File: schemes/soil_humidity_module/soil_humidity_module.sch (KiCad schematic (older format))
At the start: 10 parts, among them Q1 IRL540N, Q2 BC547, U1 nRF24L01P, U2 SEN0193

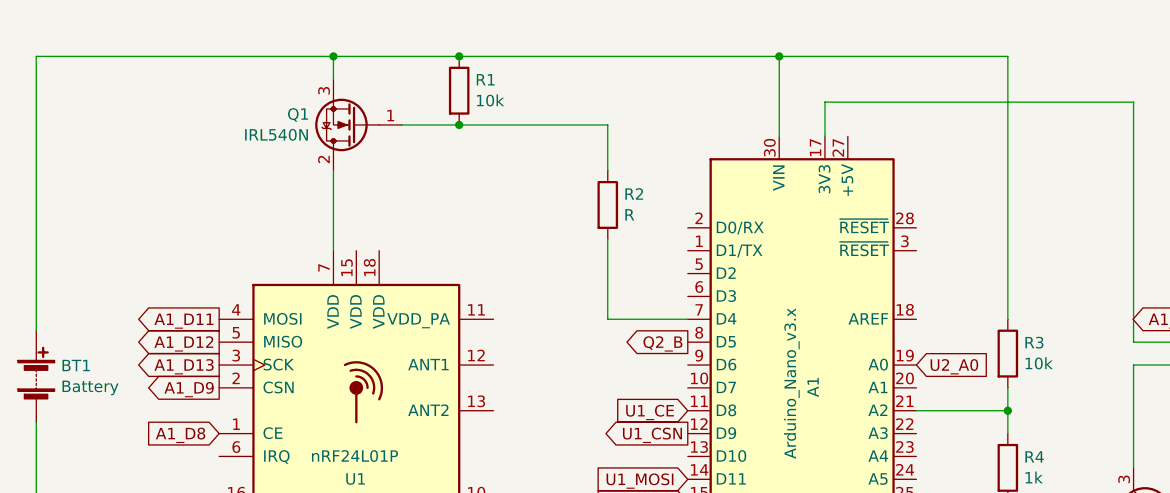
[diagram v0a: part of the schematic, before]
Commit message: Added weekdays selection popup. Changed front-end file structure
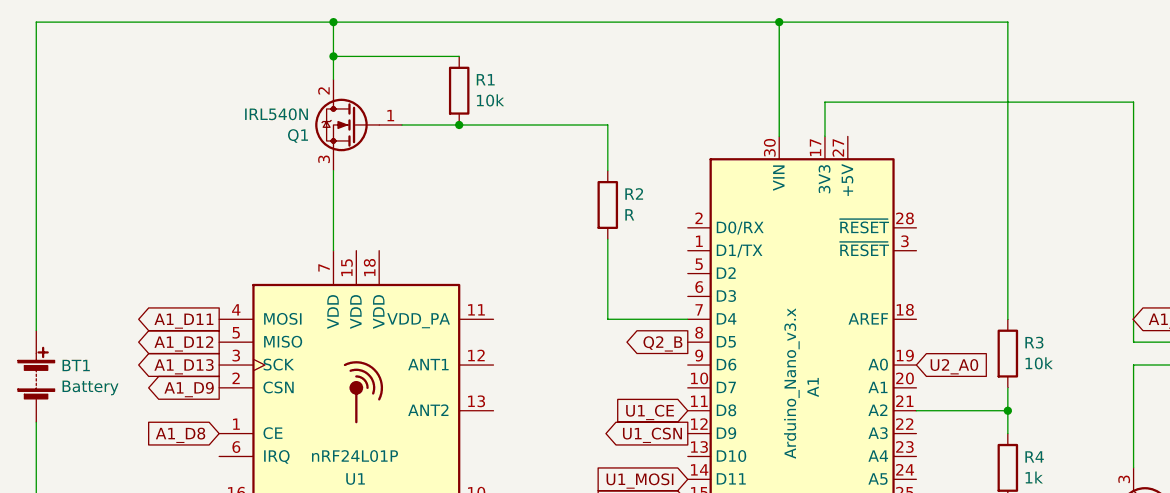
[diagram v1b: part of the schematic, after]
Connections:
- net at A1.30 (VIN), BT1.1 (+), R1.1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: now also Q1.2 (D); no longer Q1.3 (S)
- net at U1.7 (VDD): now also Q1.3 (S); no longer Q1.2 (D)
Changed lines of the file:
@@
 U1_CE
-Wire Wire Line
-	3300 2600 3300 3800
 Wire Wire Line
 	3300 5150 4600 5150
@@
 	6650 5150 6650 4950
 Connection ~ 4600 5150
-Wire Wire Line
-	6550 2600 6550 2950
 $Comp
 L Device:R R3
@@
 	7550 5150 7550 4550
 Connection ~ 6650 5150
-Connection ~ 6550 2600
-Wire Wire Line
-	7550 2600 7550 3750
 Wire Wire Line
 	7550 4050 7550 4150
@@
 Wire Wire Line
 	5800 3750 6150 3750
-Wire Wire Line
-	3300 2600 4600 2600
-Connection ~ 4600 2600
-Wire Wire Line
-	4600 2600 5150 2600
 $Comp
 L Device:R R1
@@
 	1    0    0    -1
 $EndComp
-Connection ~ 5150 2600
 Wire Wire Line
 	4600 2700 4600 2600
@@
 F 3 "https://www.infineon.com/dgdl/irl540npbf.pdf?fileId=5546d462533600a40153565fc2a62567" H 4700 2900 50  0001 L CNN
 	1    4700 2900
-	-1   0    0    1
+	-1   0    0    -1
 $EndComp
 Wire Wire Line
@@
 Wire Wire Line
 	4600 5150 6650 5150
-Wire Wire Line
-	5150 2600 6550 2600
 $Comp
 L trial:SEN0193 U2
@@
 Text GLabel 7150 3950 2    50   Input ~ 0
 U2_A0
-Wire Wire Line
-	6550 2600 7550 2600
 Wire Wire Line
 	6650 5150 7550 5150
@@
 	1    0    0    -1
 $EndComp
+Wire Wire Line
+	3300 2450 4600 2450
+Wire Wire Line
+	3300 2450 3300 3800
+Wire Wire Line
+	7550 2450 7550 3750
+Wire Wire Line
+	6550 2450 6550 2950
+Connection ~ 6550 2450
+Wire Wire Line
+	6550 2450 7550 2450
+Wire Wire Line
+	5150 2600 4600 2600
+Wire Wire Line
+	4600 2600 4600 2450
+Connection ~ 4600 2600
+Connection ~ 4600 2450
+Wire Wire Line
+	4600 2450 6550 2450
 $EndSCHEMATC

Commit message: Updated schemes and technical sheets
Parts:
- removed R2: R, symbol Device:R
- R1: value 10k -> 100k
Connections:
- net at A1.18 (AREF): now also A1.27 (+5V)
- net at A1.29 (GND): now also A1.4 (GND), BT1.2 (-), Q1.3 (S), Q2.3 (E), R1.2, R4.2
- net at A1.30 (VIN), BT1.1 (+), R3.1: now also U1.7 (VDD); no longer Q1.2 (D), R1.1
- net at A1.7 (D4): now also Q1.1 (G), R1.1
- net at U2.1 (GND): now also Q2.1 (C); no longer Q2.3 (E)
- net U1_D5 renamed A1_D5
- new net: Q1.2 (D), U1.8 (VSS)
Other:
- moved on the sheet: Q1, R1, U1
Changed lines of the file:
@@
 Text GLabel 6150 4550 0    50   Input ~ 0
 U1_MISO
-Text GLabel 4100 3850 0    50   Output ~ 0
-A1_D12
-Text GLabel 4100 3950 0    50   Output ~ 0
-A1_D13
-Text GLabel 6150 4650 0    50   Input ~ 0
+Text GLabel 6150 4650 0    50   Output ~ 0
 U1_SCK
-Text GLabel 6150 4450 0    50   Input ~ 0
+Text GLabel 6150 4450 0    50   Output ~ 0
 U1_MOSI
-Text GLabel 4100 3750 0    50   Output ~ 0
-A1_D11
-Text GLabel 4100 4050 0    50   Output ~ 0
-A1_D9
 Text GLabel 6150 4250 0    50   Output ~ 0
 U1_CSN
-Text GLabel 4100 4250 0    50   Input ~ 0
-A1_D8
-Text GLabel 6150 4150 0    50   Input ~ 0
+Text GLabel 6150 4150 0    50   Output ~ 0
 U1_CE
-Wire Wire Line
-	3300 5150 4600 5150
-Wire Wire Line
-	3300 4200 3300 5150
-Wire Wire Line
-	4600 5050 4600 5150
-Wire Wire Line
-	6650 5150 6650 4950
-Connection ~ 4600 5150
 $Comp
 L Device:R R3
@@
 $EndComp
 Wire Wire Line
-	7550 5150 7550 4550
-Connection ~ 6650 5150
-Wire Wire Line
 	7550 4050 7550 4150
 Connection ~ 7550 4150
@@
 	7550 4150 7550 4250
 Wire Wire Line
-	5800 3750 6150 3750
-$Comp
-L Device:R R1
-U 1 1 5F31B617
-P 5150 2750
-F 0 "R1" H 5220 2796 50  0000 L CNN
-F 1 "10k" H 5220 2705 50  0000 L CNN
-F 2 "" V 5080 2750 50  0001 C CNN
-F 3 "~" H 5150 2750 50  0001 C CNN
-	1    5150 2750
-	1    0    0    -1
-$EndComp
-Wire Wire Line
-	4600 2700 4600 2600
-Wire Wire Line
-	4600 3100 4600 3450
-$Comp
-L trial:IRL540N Q1
-U 1 1 5F29F1A2
-P 4700 2900
-F 0 "Q1" H 4905 2854 50  0000 L CNN
-F 1 "IRL540N" H 4905 2945 50  0000 L CNN
-F 2 "Package_TO_SOT_THT:TO-220-3_Vertical" H 4950 2825 50  0001 L CIN
-F 3 "https://www.infineon.com/dgdl/irl540npbf.pdf?fileId=5546d462533600a40153565fc2a62567" H 4700 2900 50  0001 L CNN
-	1    4700 2900
-	-1   0    0    -1
-$EndComp
-Wire Wire Line
-	4900 2900 5150 2900
-Wire Wire Line
-	5800 2900 5800 3100
-Connection ~ 5150 2900
-Wire Wire Line
-	5150 2900 5800 2900
-$Comp
-L Device:R R2
-U 1 1 5F322358
-P 5800 3250
-F 0 "R2" H 5870 3296 50  0000 L CNN
-F 1 "R" H 5870 3205 50  0000 L CNN
-F 2 "" V 5730 3250 50  0001 C CNN
-F 3 "~" H 5800 3250 50  0001 C CNN
-	1    5800 3250
-	1    0    0    -1
-$EndComp
-Wire Wire Line
-	5800 3400 5800 3750
-Wire Wire Line
 	7150 4150 7550 4150
-Wire Wire Line
-	4600 5150 6650 5150
 $Comp
 L trial:SEN0193 U2
@@
 U2_A0
 Wire Wire Line
-	6650 5150 7550 5150
-Wire Wire Line
 	6750 2950 6750 2800
 Wire Wire Line
@@
 F 3 "http://www.fairchildsemi.com/ds/BC/BC547.pdf" H 8200 4600 50  0001 L CNN
 	1    8200 4600
-	-1   0    0    1
+	-1   0    0    -1
 $EndComp
-Text GLabel 8400 4600 2    50   Input ~ 0
-U1_D5
 Text GLabel 6150 3850 0    50   Output ~ 0
 Q2_B
 Wire Wire Line
-	8100 4800 8100 5150
-Wire Wire Line
 	6750 2800 8100 2800
 Wire Wire Line
-	7550 5150 8100 5150
-Connection ~ 7550 5150
+	3300 2650 4650 2650
+Wire Wire Line
+	4650 5300 5100 5300
+Connection ~ 4650 5300
+Wire Wire Line
+	3300 5300 4650 5300
+Wire Wire Line
+	4650 5300 4650 5200
+Wire Wire Line
+	5100 5300 6650 5300
+Connection ~ 5100 5300
+Wire Wire Line
+	5100 5000 5550 5000
+Connection ~ 5100 5000
+Wire Wire Line
+	4950 5000 5100 5000
+$Comp
+L trial:IRL540N Q1
+U 1 1 5F29F1A2
+P 4750 5000
+F 0 "Q1" H 4955 4954 50  0000 L CNN
+F 1 "IRL540N" H 4955 5045 50  0000 L CNN
+F 2 "Package_TO_SOT_THT:TO-220-3_Vertical" H 5000 4925 50  0001 L CIN
+F 3 "https://www.infineon.com/dgdl/irl540npbf.pdf?fileId=5546d462533600a40153565fc2a62567" H 4750 5000 50  0001 L CNN
+	1    4750 5000
+	-1   0    0    -1
+$EndComp
 $Comp
 L RF:nRF24L01P U1
 U 1 1 5F26A887
-P 4700 4250
-F 0 "U1" H 4650 4050 50  0000 L CNN
-F 1 "nRF24L01P" H 4500 4150 50  0000 L CNN
-F 2 "Package_DFN_QFN:QFN-20-1EP_4x4mm_P0.5mm_EP2.5x2.5mm" V 4609 5093 50  0001 L CIN
-F 3 "http://www.nordicsemi.com/eng/content/download/2726/34069/file/nRF24L01P_Product_Specification_1_0.pdf" H 4700 4350 50  0001 C CNN
-	1    4700 4250
+P 4750 3900
+F 0 "U1" H 4700 3700 50  0000 L CNN
+F 1 "nRF24L01P" H 4550 3800 50  0000 L CNN
+F 2 "Package_DFN_QFN:QFN-20-1EP_4x4mm_P0.5mm_EP2.5x2.5mm" V 4659 4743 50  0001 L CIN
+F 3 "http://www.nordicsemi.com/eng/content/download/2726/34069/file/nRF24L01P_Product_Specification_1_0.pdf" H 4750 4000 50  0001 C CNN
+	1    4750 3900
+	1    0    0    -1
+$EndComp
+$Comp
+L Device:R R1
+U 1 1 5F31B617
+P 5100 5150
+F 0 "R1" H 5170 5196 50  0000 L CNN
+F 1 "100k" H 5170 5105 50  0000 L CNN
+F 2 "" V 5030 5150 50  0001 C CNN
+F 3 "~" H 5100 5150 50  0001 C CNN
+	1    5100 5150
 	1    0    0    -1
 $EndComp
 Wire Wire Line
-	3300 2450 4600 2450
+	4650 4700 4650 4800
+Text GLabel 4150 3900 0    50   Input ~ 0
+A1_D8
+Text GLabel 4150 3700 0    50   Input ~ 0
+A1_D9
+Text GLabel 4150 3400 0    50   Input ~ 0
+A1_D11
+Text GLabel 4150 3600 0    50   Input ~ 0
+A1_D13
+Text GLabel 4150 3500 0    50   Output ~ 0
+A1_D12
 Wire Wire Line
-	3300 2450 3300 3800
+	5550 3750 6150 3750
 Wire Wire Line
-	7550 2450 7550 3750
+	6650 4950 6650 5300
+Connection ~ 6650 5300
 Wire Wire Line
-	6550 2450 6550 2950
-Connection ~ 6550 2450
+	6650 5300 6750 5300
 Wire Wire Line
-	6550 2450 7550 2450
+	7550 4550 7550 5300
+Connection ~ 7550 5300
 Wire Wire Line
-	5150 2600 4600 2600
+	7550 5300 8100 5300
 Wire Wire Line
-	4600 2600 4600 2450
-Connection ~ 4600 2600
-Connection ~ 4600 2450
+	8100 4800 8100 5300
+Text GLabel 8400 4600 2    50   Input ~ 0
+A1_D5
 Wire Wire Line
-	4600 2450 6550 2450
+	3300 4200 3300 5300
+Wire Wire Line
+	4650 2650 6550 2650
+Connection ~ 4650 2650
+Wire Wire Line
+	4650 2650 4650 3100
+Connection ~ 6550 2650
+Wire Wire Line
+	6550 2650 6550 2950
+Wire Wire Line
+	7550 2650 7550 3750
+Wire Wire Line
+	3300 2650 3300 3800
+Wire Wire Line
+	5550 3750 5550 5000
+Wire Wire Line
+	6750 4950 6750 5300
+Connection ~ 6750 5300
+Wire Wire Line
+	6750 5300 7550 5300
+Wire Wire Line
+	6550 2650 7550 2650
+Wire Wire Line
+	6850 2950 6850 2900
+Wire Wire Line
+	6850 2900 7350 2900
+Wire Wire Line
+	7350 2900 7350 3750
+Wire Wire Line
+	7350 3750 7150 3750
 $EndSCHEMATC

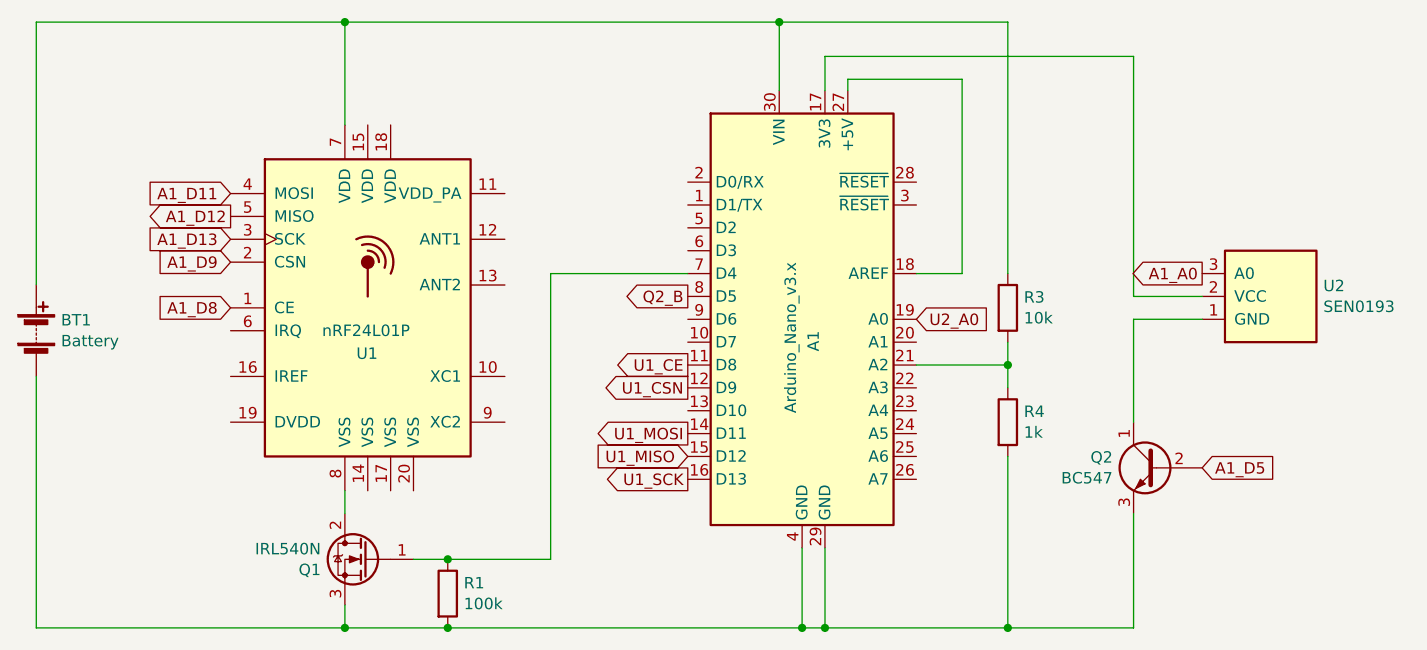
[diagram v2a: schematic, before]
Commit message: Improving soil humidity module scheme and pcb
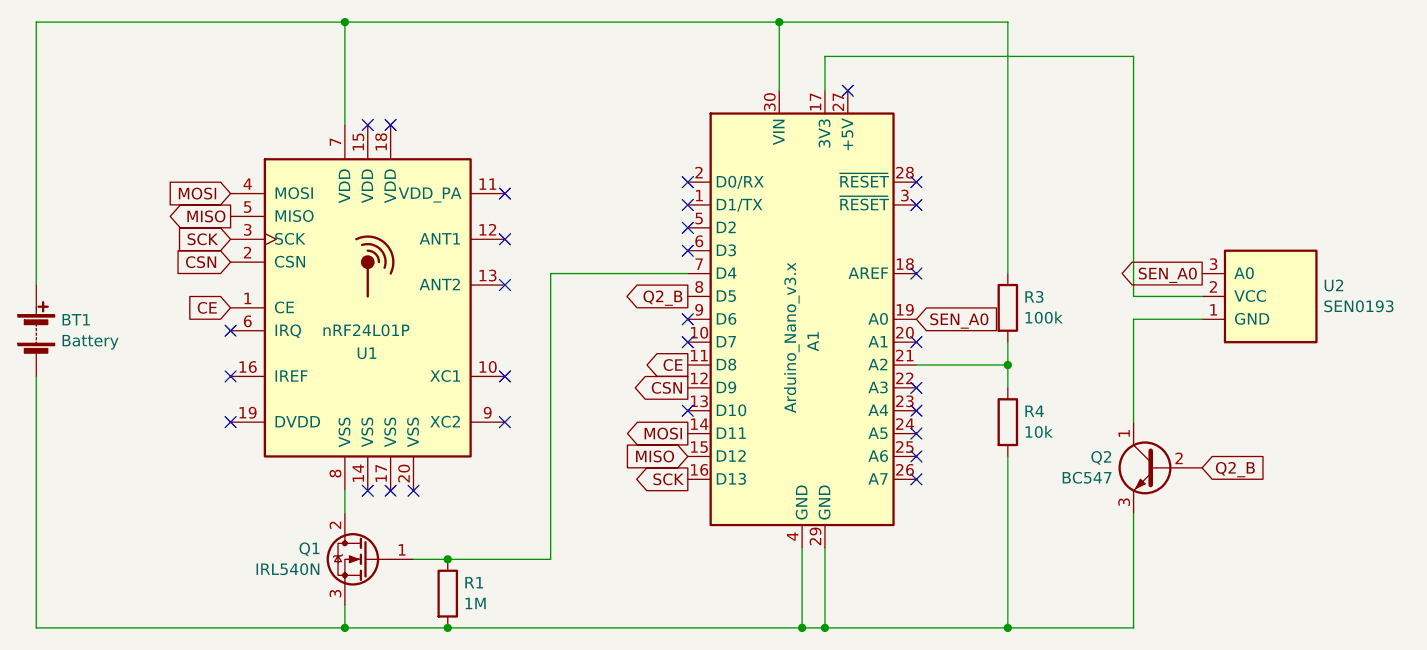
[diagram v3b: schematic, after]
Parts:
- removed Q1: IRL540N, Package_TO_SOT_THT:TO-220-3_Vertical, symbol trial:IRL540N
- added Q1: IRL540N, Package_TO_SOT_THT:TO-220-3_Vertical, symbol soil_humidity_module:IRL540N
- BT1: footprint (none) -> Connector_AMASS:AMASS_XT30U-F_1x02_P5.0mm_Vertical
- R1: value 100k -> 1M; footprint (none) -> Resistor_SMD:R_0805_2012Metric_Pad1.15x1.40mm_HandSolder
- R3: value 10k -> 100k; footprint (none) -> Resistor_SMD:R_0805_2012Metric_Pad1.15x1.40mm_HandSolder
- R4: value 1k -> 10k; footprint (none) -> Resistor_SMD:R_0805_2012Metric_Pad1.15x1.40mm_HandSolder
- U1: footprint Package_DFN_QFN:QFN-20-1EP_4x4mm_P0.5mm_EP2.5x2.5mm -> Connector_PinHeader_2.54mm:PinHeader_2x04_P2.54mm_Vertical
- U2: footprint (none) -> Connector_JST:JST_EH_B3B-EH-A_1x03_P2.50mm_Vertical
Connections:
- net A1_D5 is gone; now on net Q2_B: Q2.2 (B)
- net U1_CE is gone; now on net CE: A1.11 (D8)
- net U1_CSN is gone; now on net CSN: A1.12 (D9)
- net U1_MISO is gone; now on net MISO: A1.15 (D12)
- net U1_MOSI is gone; now on net MOSI: A1.14 (D11)
- net U1_SCK is gone; now on net SCK: A1.16 (D13)
- net U2_A0 is gone; now on net SEN_A0: A1.19 (A0)
- net at A1.18 (AREF): no longer A1.27 (+5V)
- net at A1.29 (GND), A1.4 (GND), BT1.2 (-)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: now also Q1.3 (S)
- net at A1.7 (D4), R1.1: now also Q1.1 (G)
- net at U1.8 (VSS): now also Q1.2 (D)
- net A1_A0 renamed SEN_A0
- net A1_D11 renamed MOSI
- net A1_D12 renamed MISO
- net A1_D13 renamed SCK
- net A1_D8 renamed CE
- net A1_D9 renamed CSN
- no-connect marks 0 -> 30
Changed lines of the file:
@@
 F 0 "BT1" H 3408 4046 50  0000 L CNN
 F 1 "Battery" H 3408 3955 50  0000 L CNN
-F 2 "" V 3300 4060 50  0001 C CNN
+F 2 "Connector_AMASS:AMASS_XT30U-F_1x02_P5.0mm_Vertical" V 3300 4060 50  0001 C CNN
 F 3 "~" V 3300 4060 50  0001 C CNN
 	1    3300 4000
@@
 $EndComp
 Text GLabel 6150 4550 0    50   Input ~ 0
-U1_MISO
+MISO
 Text GLabel 6150 4650 0    50   Output ~ 0
-U1_SCK
+SCK
 Text GLabel 6150 4450 0    50   Output ~ 0
-U1_MOSI
+MOSI
 Text GLabel 6150 4250 0    50   Output ~ 0
-U1_CSN
+CSN
 Text GLabel 6150 4150 0    50   Output ~ 0
-U1_CE
+CE
 $Comp
 L Device:R R3
@@
 P 7550 3900
 F 0 "R3" H 7620 3946 50  0000 L CNN
-F 1 "10k" H 7620 3855 50  0000 L CNN
-F 2 "" V 7480 3900 50  0001 C CNN
+F 1 "100k" H 7620 3855 50  0000 L CNN
+F 2 "Resistor_SMD:R_0805_2012Metric_Pad1.15x1.40mm_HandSolder" V 7480 3900 50  0001 C CNN
 F 3 "~" H 7550 3900 50  0001 C CNN
 	1    7550 3900
@@
 P 7550 4400
 F 0 "R4" H 7620 4446 50  0000 L CNN
-F 1 "1k" H 7620 4355 50  0000 L CNN
-F 2 "" V 7480 4400 50  0001 C CNN
+F 1 "10k" H 7620 4355 50  0000 L CNN
+F 2 "Resistor_SMD:R_0805_2012Metric_Pad1.15x1.40mm_HandSolder" V 7480 4400 50  0001 C CNN
 F 3 "~" H 7550 4400 50  0001 C CNN
 	1    7550 4400
@@
 F 0 "U2" V 8646 3520 50  0000 R CNN
 F 1 "SEN0193" V 8555 3520 50  0000 R CNN
-F 2 "" H 8500 3450 50  0001 C CNN
+F 2 "Connector_JST:JST_EH_B3B-EH-A_1x03_P2.50mm_Vertical" H 8500 3450 50  0001 C CNN
 F 3 "" H 8500 3450 50  0001 C CNN
 	1    8600 3850
@@
 	8100 3850 8100 2800
 Text GLabel 8400 3750 0    50   Output ~ 0
-A1_A0
+SEN_A0
 Wire Wire Line
 	8100 3850 8400 3850
@@
 	8100 3950 8400 3950
 Text GLabel 7150 3950 2    50   Input ~ 0
-U2_A0
+SEN_A0
 Wire Wire Line
 	6750 2950 6750 2800
@@
 	6750 2800 8100 2800
 Wire Wire Line
-	3300 2650 4650 2650
-Wire Wire Line
 	4650 5300 5100 5300
-Connection ~ 4650 5300
-Wire Wire Line
-	3300 5300 4650 5300
 Wire Wire Line
 	4650 5300 4650 5200
-Wire Wire Line
-	5100 5300 6650 5300
 Connection ~ 5100 5300
 Wire Wire Line
@@
 Wire Wire Line
 	4950 5000 5100 5000
-$Comp
-L trial:IRL540N Q1
-U 1 1 5F29F1A2
-P 4750 5000
-F 0 "Q1" H 4955 4954 50  0000 L CNN
-F 1 "IRL540N" H 4955 5045 50  0000 L CNN
-F 2 "Package_TO_SOT_THT:TO-220-3_Vertical" H 5000 4925 50  0001 L CIN
-F 3 "https://www.infineon.com/dgdl/irl540npbf.pdf?fileId=5546d462533600a40153565fc2a62567" H 4750 5000 50  0001 L CNN
-	1    4750 5000
-	-1   0    0    -1
-$EndComp
 $Comp
 L RF:nRF24L01P U1
@@
 F 0 "U1" H 4700 3700 50  0000 L CNN
 F 1 "nRF24L01P" H 4550 3800 50  0000 L CNN
-F 2 "Package_DFN_QFN:QFN-20-1EP_4x4mm_P0.5mm_EP2.5x2.5mm" V 4659 4743 50  0001 L CIN
+F 2 "Connector_PinHeader_2.54mm:PinHeader_2x04_P2.54mm_Vertical" V 4659 4743 50  0001 L CIN
 F 3 "http://www.nordicsemi.com/eng/content/download/2726/34069/file/nRF24L01P_Product_Specification_1_0.pdf" H 4750 4000 50  0001 C CNN
 	1    4750 3900
@@
 P 5100 5150
 F 0 "R1" H 5170 5196 50  0000 L CNN
-F 1 "100k" H 5170 5105 50  0000 L CNN
-F 2 "" V 5030 5150 50  0001 C CNN
+F 1 "1M" H 5170 5105 50  0000 L CNN
+F 2 "Resistor_SMD:R_0805_2012Metric_Pad1.15x1.40mm_HandSolder" V 5030 5150 50  0001 C CNN
 F 3 "~" H 5100 5150 50  0001 C CNN
 	1    5100 5150
@@
 	4650 4700 4650 4800
 Text GLabel 4150 3900 0    50   Input ~ 0
-A1_D8
+CE
 Text GLabel 4150 3700 0    50   Input ~ 0
-A1_D9
+CSN
 Text GLabel 4150 3400 0    50   Input ~ 0
-A1_D11
+MOSI
 Text GLabel 4150 3600 0    50   Input ~ 0
-A1_D13
+SCK
 Text GLabel 4150 3500 0    50   Output ~ 0
-A1_D12
+MISO
 Wire Wire Line
 	5550 3750 6150 3750
-Wire Wire Line
-	6650 4950 6650 5300
-Connection ~ 6650 5300
-Wire Wire Line
-	6650 5300 6750 5300
 Wire Wire Line
 	7550 4550 7550 5300
@@
 	8100 4800 8100 5300
 Text GLabel 8400 4600 2    50   Input ~ 0
-A1_D5
+Q2_B
+Wire Wire Line
+	7550 2650 7550 3750
+Wire Wire Line
+	3300 2650 3300 3800
+Wire Wire Line
+	5550 3750 5550 5000
+$Comp
+L soil_humidity_module:IRL540N Q1
+U 1 1 5F3D6F3F
+P 4750 5000
+F 0 "Q1" H 4955 5046 50  0000 L CNN
+F 1 "IRL540N" H 4955 4955 50  0000 L CNN
+F 2 "Package_TO_SOT_THT:TO-220-3_Vertical" H 5000 4925 50  0001 L CIN
+F 3 "" H 4750 5000 50  0001 L CNN
+	1    4750 5000
+	-1   0    0    -1
+$EndComp
+NoConn ~ 6150 4350
+NoConn ~ 6150 4050
+NoConn ~ 6150 3950
+NoConn ~ 6150 3650
+NoConn ~ 6150 3550
+NoConn ~ 6150 3450
+NoConn ~ 6150 3350
+NoConn ~ 6850 2950
+NoConn ~ 7150 3350
+NoConn ~ 7150 3450
+NoConn ~ 7150 3750
+NoConn ~ 7150 4050
+NoConn ~ 7150 4250
+NoConn ~ 7150 4350
+NoConn ~ 7150 4450
+NoConn ~ 7150 4550
+NoConn ~ 7150 4650
+NoConn ~ 5350 4400
+NoConn ~ 4750 4700
+NoConn ~ 4850 4700
+NoConn ~ 4950 4700
+NoConn ~ 5350 4200
+NoConn ~ 5350 3800
+NoConn ~ 5350 3600
+NoConn ~ 5350 3400
+NoConn ~ 4850 3100
+NoConn ~ 4750 3100
+NoConn ~ 4150 4000
+NoConn ~ 4150 4200
+NoConn ~ 4150 4400
+Connection ~ 4650 5300
 Wire Wire Line
 	3300 4200 3300 5300
 Wire Wire Line
+	3300 5300 4650 5300
+Connection ~ 6650 5300
+Wire Wire Line
+	5100 5300 6650 5300
+Wire Wire Line
+	6650 4950 6650 5300
+Connection ~ 6750 5300
+Wire Wire Line
+	6750 5300 7550 5300
+Wire Wire Line
+	6650 5300 6750 5300
+Wire Wire Line
+	6750 4950 6750 5300
+Wire Wire Line
+	6550 2650 7550 2650
+Connection ~ 6550 2650
+Wire Wire Line
+	6550 2650 6550 2950
+Connection ~ 4650 2650
+Wire Wire Line
 	4650 2650 6550 2650
-Connection ~ 4650 2650
-Wire Wire Line
-	4650 2650 4650 3100
-Connection ~ 6550 2650
-Wire Wire Line
-	6550 2650 6550 2950
-Wire Wire Line
-	7550 2650 7550 3750
-Wire Wire Line
-	3300 2650 3300 3800
-Wire Wire Line
-	5550 3750 5550 5000
-Wire Wire Line
-	6750 4950 6750 5300
-Connection ~ 6750 5300
-Wire Wire Line
-	6750 5300 7550 5300
-Wire Wire Line
-	6550 2650 7550 2650
-Wire Wire Line
-	6850 2950 6850 2900
-Wire Wire Line
-	6850 2900 7350 2900
-Wire Wire Line
-	7350 2900 7350 3750
-Wire Wire Line
-	7350 3750 7150 3750
+Wire Wire Line
+	3300 2650 4650 2650
+Wire Wire Line
+	4650 3100 4650 2650
 $EndSCHEMATC
